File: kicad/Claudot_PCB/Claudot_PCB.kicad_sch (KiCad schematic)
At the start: 0 parts

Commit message: Place switches and diodes (no routing)
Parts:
- added D1, D10, D11, D2, D3, D4, D5, D6, D7, D8, D9: D_Small, Library:SOD323, symbol Device:D_Small
- added SW1, SW10, SW11, SW2, SW3, SW4, SW5, SW6, SW7, SW8, SW9: SW_Push, Library:CPG151101S11-16, symbol Switch:SW_Push
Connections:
- new net: D7.2 (A), SW7.2
- new net: D4.2 (A), SW4.2
- new net: D6.2 (A), SW6.2
- new net: D1.2 (A), SW1.2
- new net: D5.2 (A), SW5.2
- new net: D10.2 (A), SW10.2
- new net: D11.2 (A), SW11.2
- new net: D2.2 (A), SW2.2
- new net: D9.2 (A), SW9.2
- new net: D8.2 (A), SW8.2
- new net: D3.2 (A), SW3.2

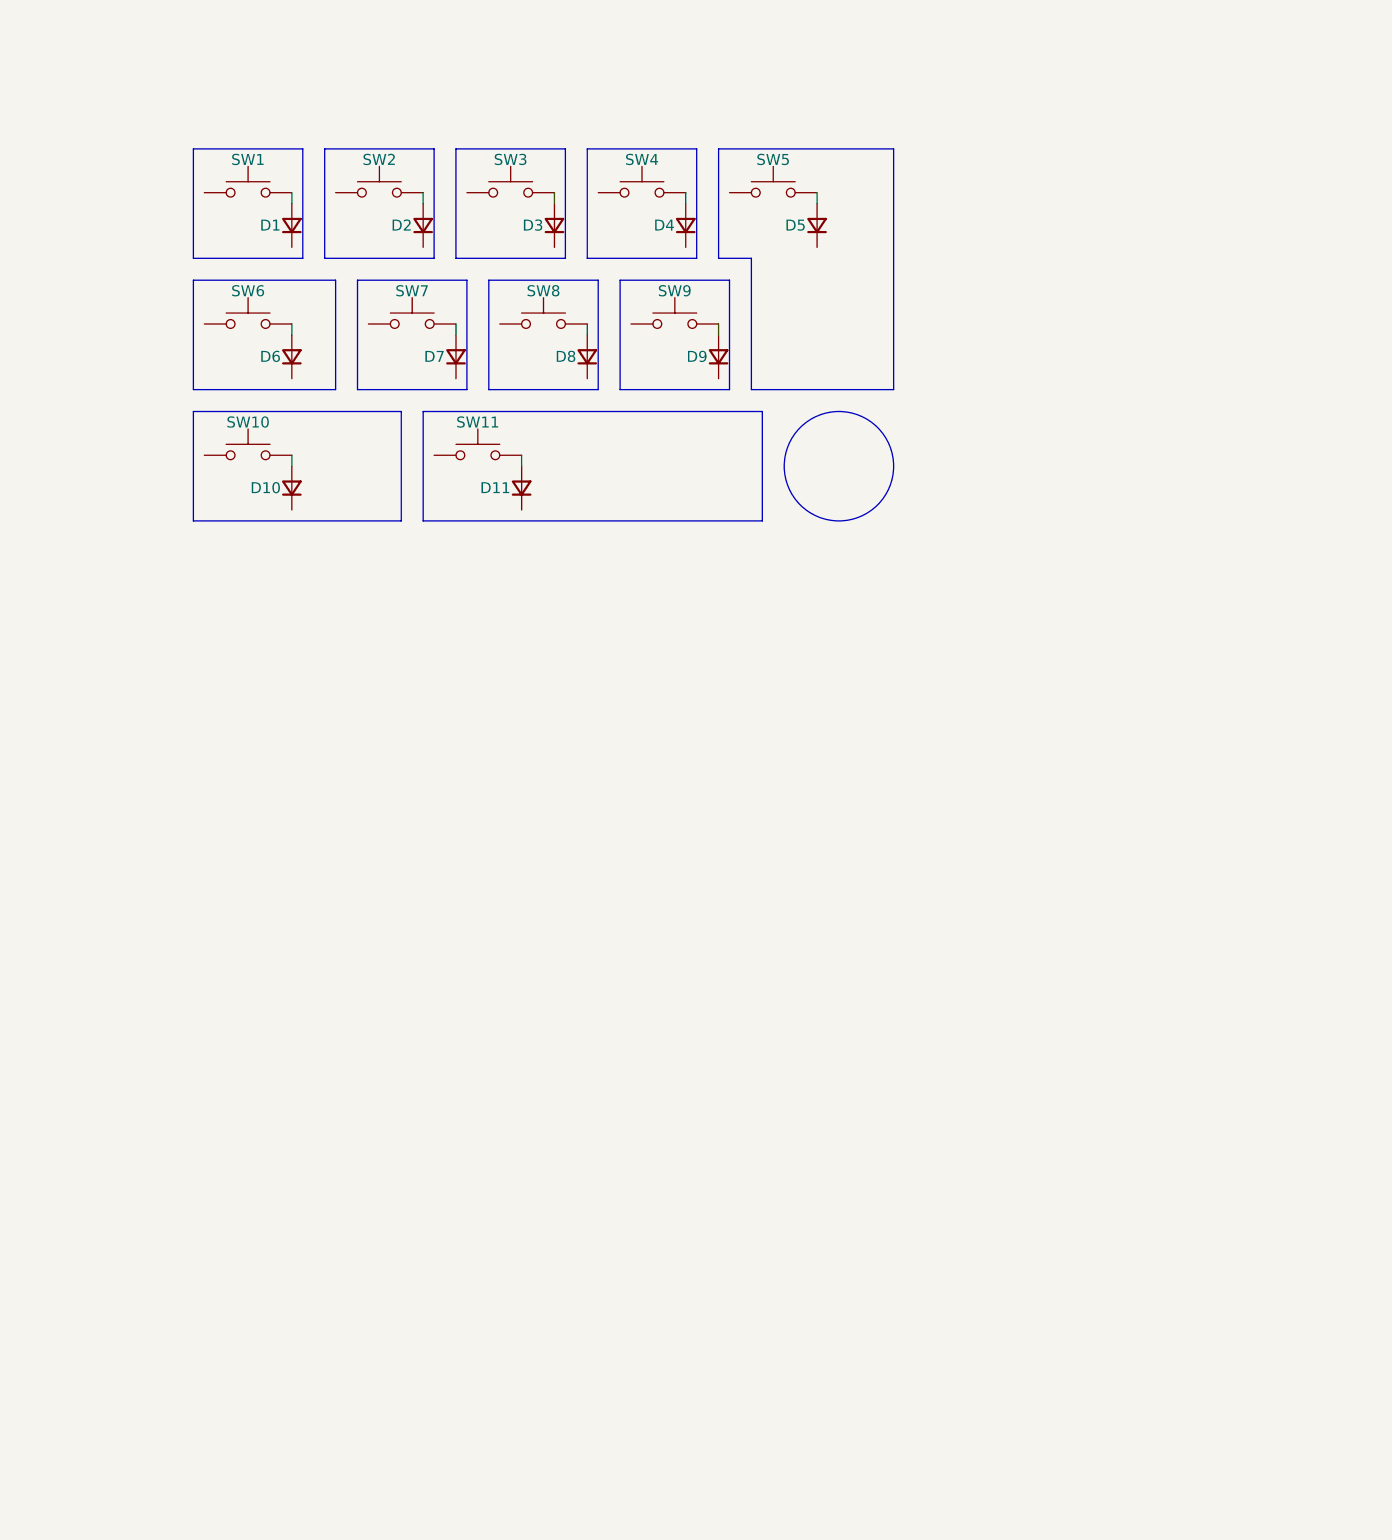
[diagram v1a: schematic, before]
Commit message: Place ICs and rotary encoder
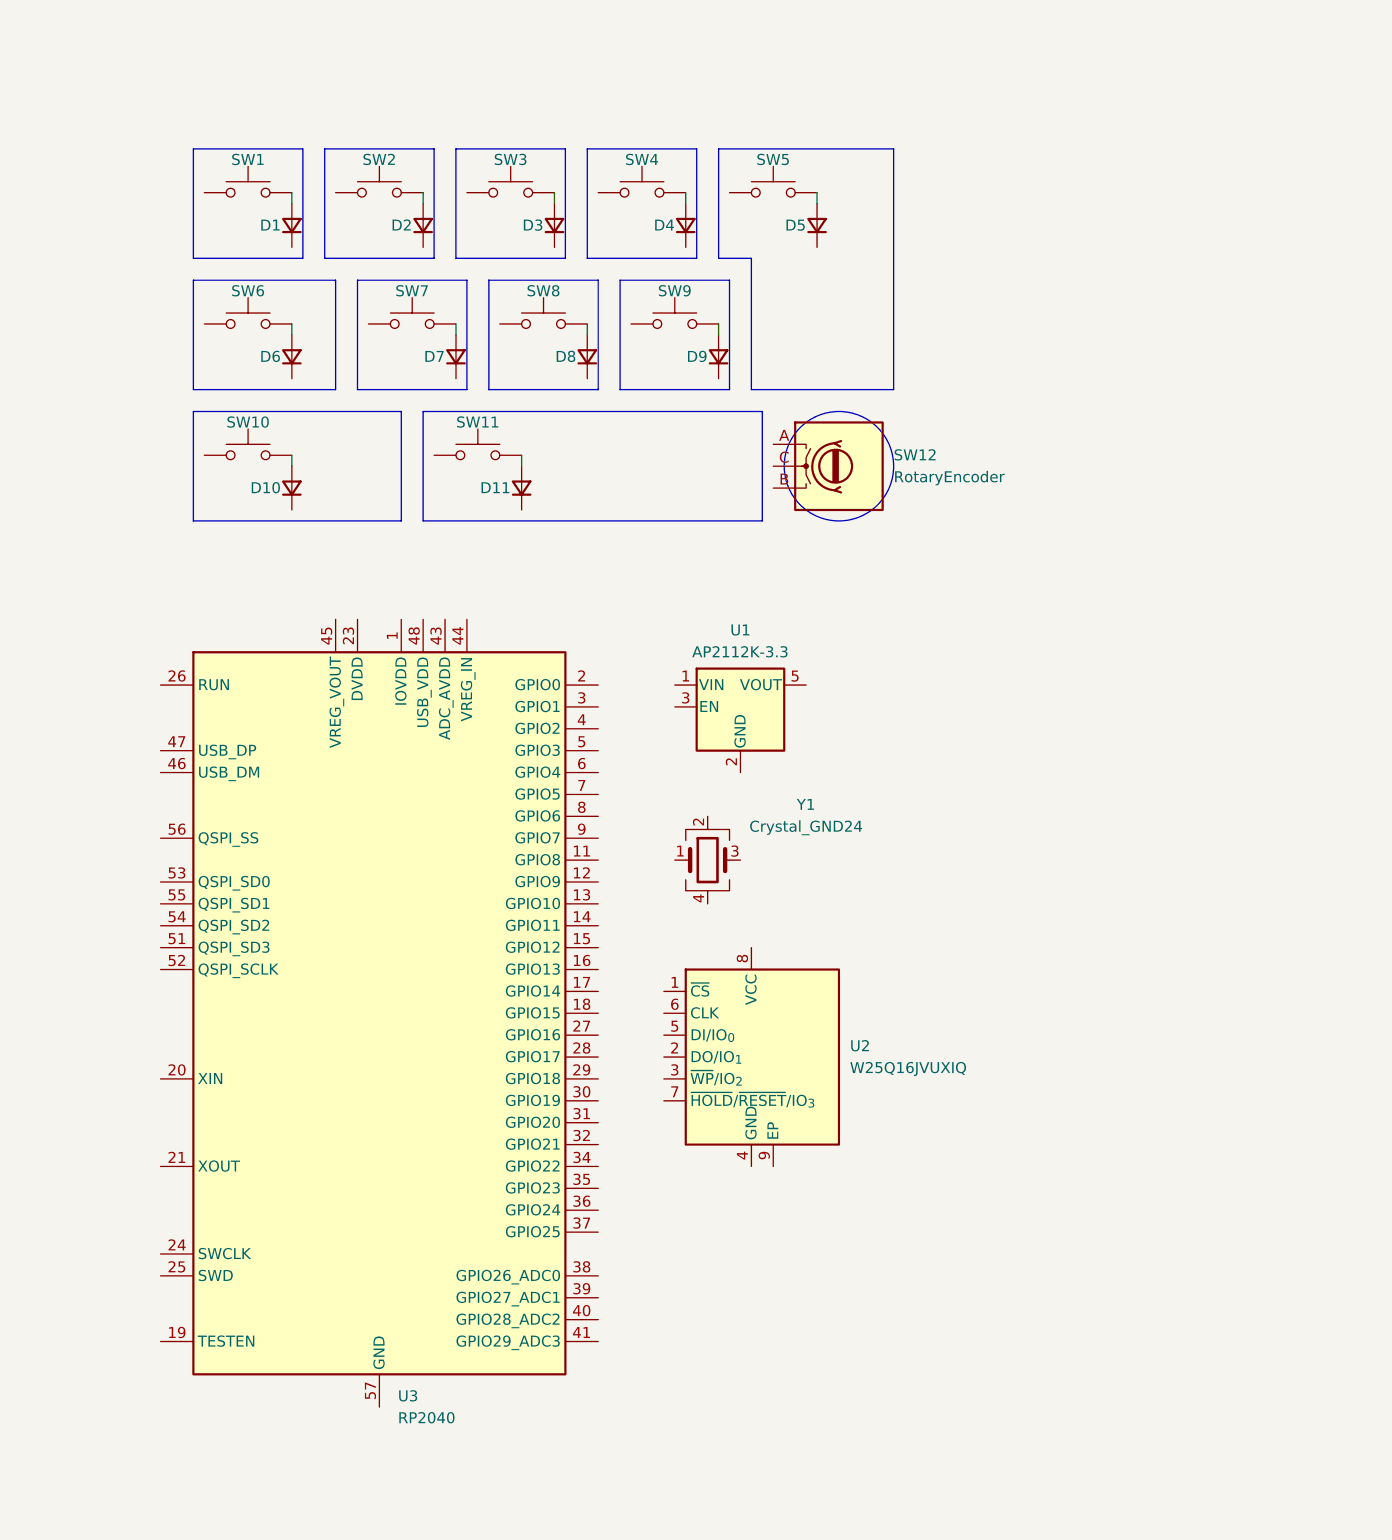
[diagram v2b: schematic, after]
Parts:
- added SW12: RotaryEncoder, Rotary_Encoder:RotaryEncoder_Alps_EC12E_Vertical_H20mm, symbol Device:RotaryEncoder
- added U1: AP2112K-3.3, Library:SOT25, symbol Regulator_Linear:AP2112K-3.3
- added U2: W25Q16JVUXIQ, Library:W25Q16JVUXIQ, symbol Library:W25Q16JVUXIQ
- added U3: RP2040, Library:RP2040, symbol MCU_RaspberryPi:RP2040
- added Y1: Crystal_GND24, Crystal:Crystal_SMD_3225-4Pin_3.2x2.5mm, symbol Device:Crystal_GND24
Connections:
- new net: U3.1 (IOVDD), U3.10 (IOVDD), U3.22 (IOVDD), U3.33 (IOVDD), U3.42 (IOVDD), U3.49 (IOVDD)
- new net: U3.23 (DVDD), U3.50 (DVDD)

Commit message: Update schematic and pcb
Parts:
- added C1, C2: 30pF, Library:C_0402, symbol Device:C_Small
- added C10, C11, C12, C13, C14, C5, C6, C7, C8, C9: 0.1uF, Library:C_0402, symbol Device:C_Small
- added C3, C4: 1uF, Library:C_0402, symbol Device:C_Small
- added R1: 10K, Library:R_0402, symbol Device:R_Small
- added R2: 1K, Library:R_0402, symbol Device:R_Small
- Y1: value Crystal_GND24 -> 12MHz; footprint Crystal:Crystal_SMD_3225-4Pin_3.2x2.5mm -> Library:SMD3225-4P; LCSC (none) -> C9002
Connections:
- net at U2.1 (~{CS}): now also U3.56 (QSPI_SS)
- net at U2.2 (DO/IO_{1}): now also U3.55 (QSPI_SD1)
- net at U2.3 (~{WP}/IO_{2}): now also U3.54 (QSPI_SD2)
- net GND: now reaches U2.4 (GND)
- net GND: now also U3.57 (GND), Y1.2, Y1.4, C1.2, C10.2, C11.2, C12.2, C13.2, C14.2, C2.2, C3.2, C4.2, C5.2, C6.2, C7.2, C8.2, C9.2
- net at U2.5 (DI/IO_{0}): now also U3.53 (QSPI_SD0)
- net at U2.6 (CLK): now also U3.52 (QSPI_SCLK)
- net at U2.7 (~{HOLD}/~{RESET}/IO_{3}): now also U3.51 (QSPI_SD3)
- net +3V3: now reaches U2.8 (VCC)
- net +3V3: now also U3.1 (IOVDD), U3.10 (IOVDD), U3.22 (IOVDD), U3.33 (IOVDD), U3.42 (IOVDD), U3.43 (ADC_AVDD), U3.44 (VREG_IN), U3.48 (USB_VDD), U3.49 (IOVDD), C10.1, C11.1, C12.1, C3.1, C5.1, C6.1, C7.1, C8.1, C9.1, R1.1
- net at Y1.1: now also C2.1, R2.2
- net at Y1.3: now also U3.20 (XIN), C1.1
- net at U3.21 (XOUT): now also R2.1
- net +1V1: now reaches U3.23 (DVDD), U3.50 (DVDD)
- net +1V1: now also U3.45 (VREG_VOUT), C13.1, C14.1, C4.1
- net at U3.26 (RUN): now also R1.2
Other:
- note added: "Close to VREG_VIN (1uF) Close to each IOVDD, USB_VDD, ADC_AVDD"
- note added: "Close to VREG_VOUT (1uF) Close to each DVDD"
- moved on the sheet: D1, D10, D11, D2, D3, D4, D5, D6, D7, D8, D9, SW1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

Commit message: Update schematic and pcb
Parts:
- added C15, C16: 10uF, Library:C_0402, symbol Device:C_Small
- renumbered U3 to U1, U1 to U2, U2 to U3
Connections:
- net GND: now also U1.19 (TESTEN), U2.2 (GND), C15.2, C16.2
- net +5V: now reaches U2.1 (VIN)
- net +5V: now also U2.3 (EN), C15.1
- net at U2.5 (VOUT): now also C16.1
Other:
- moved on the sheet: U2

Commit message: Update schematic and pcb
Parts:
- added R5, R6: 27, Library:R_0402, symbol Device:R_Small
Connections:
- net D-: now reaches U1.46 (USB_DM)
- net D-: now also R6.1
- net D+: now reaches U1.47 (USB_DP)
- net D+: now also R5.1

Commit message: Update schematic and pcb
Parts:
- added J1: Conn_01x04, Connector_Molex:Molex_Pico-EZmate_78171-0004_1x04-1MP_P1.20mm_Vertical, symbol Connector_Generic:Conn_01x04
- added R3: 10K, Resistor_SMD:R_0402_1005Metric, symbol Device:R_Small
- added R4: 1K, Resistor_SMD:R_0402_1005Metric, symbol Device:R_Small
- renumbered U3 to U2, U2 to U3
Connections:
- net +3V3: now also C16.1, U3.5 (VOUT), R3.1
- net +5V: now also J1.1 (Pin_1)
- net D+: now also R6.2, J1.3 (Pin_3); no longer R5.1, U1.47 (USB_DP)
- net D-: now also R5.2, J1.2 (Pin_2); no longer R6.1, U1.46 (USB_DM)
- net GND: now also J1.4 (Pin_4)
- net QSPI_SS_N: now reaches U1.56 (QSPI_SS), U2.1 (~{CS})
- net QSPI_SS_N: now also R3.2, R4.1
- net ~{RESET}: now reaches R1.2, U1.26 (RUN)
- new net: R6.1, U1.47 (USB_DP)
- new net: R5.1, U1.46 (USB_DM)
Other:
- note added: "Use like Unified Daughterboard"
- moved on the sheet: C1, C10, C11, C12, C13, C14, C15, C16, C2, C3, C4, C5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

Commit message: Change J1 footprint
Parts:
- J1: footprint Connector_Molex:Molex_Pico-EZmate_78171-0004_1x04-1MP_P1.20mm_Vertical -> Library:AFC01-S04FCC-00
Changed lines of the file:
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@@
 			)
 		)
-		(property "Footprint" "Connector_Molex:Molex_Pico-EZmate_78171-0004_1x04-1MP_P1.20mm_Vertical"
+		(property "Footprint" "Library:AFC01-S04FCC-00"
 			(at 31.75 73.66 0)
 			(effects

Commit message: Update
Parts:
- added SW_B1, SW_R1: SKRP_Switch, Library:SKRP_Switch, symbol Library:SKRP_Switch
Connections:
- net GND: now also SW_B1.1, SW_R1.1
- net ~{RESET}: now also SW_R1.3
- net at R4.2: now also SW_B1.3
- net QSPI_SS_N renamed QSPI_SS
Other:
- moved on the sheet: R3, R4
